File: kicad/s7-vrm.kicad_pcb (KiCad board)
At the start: 2 copper layers, 61.5 x 53 mm, 35 parts, among them J1 Conn_02x15_Row_Letter_First, Q1 Q_NPN_BEC, Q2 Q_NMOS_GDS, Q3 Q_NMOS_GDS, SW1 SW_DIP_x04, U1 NCP1579

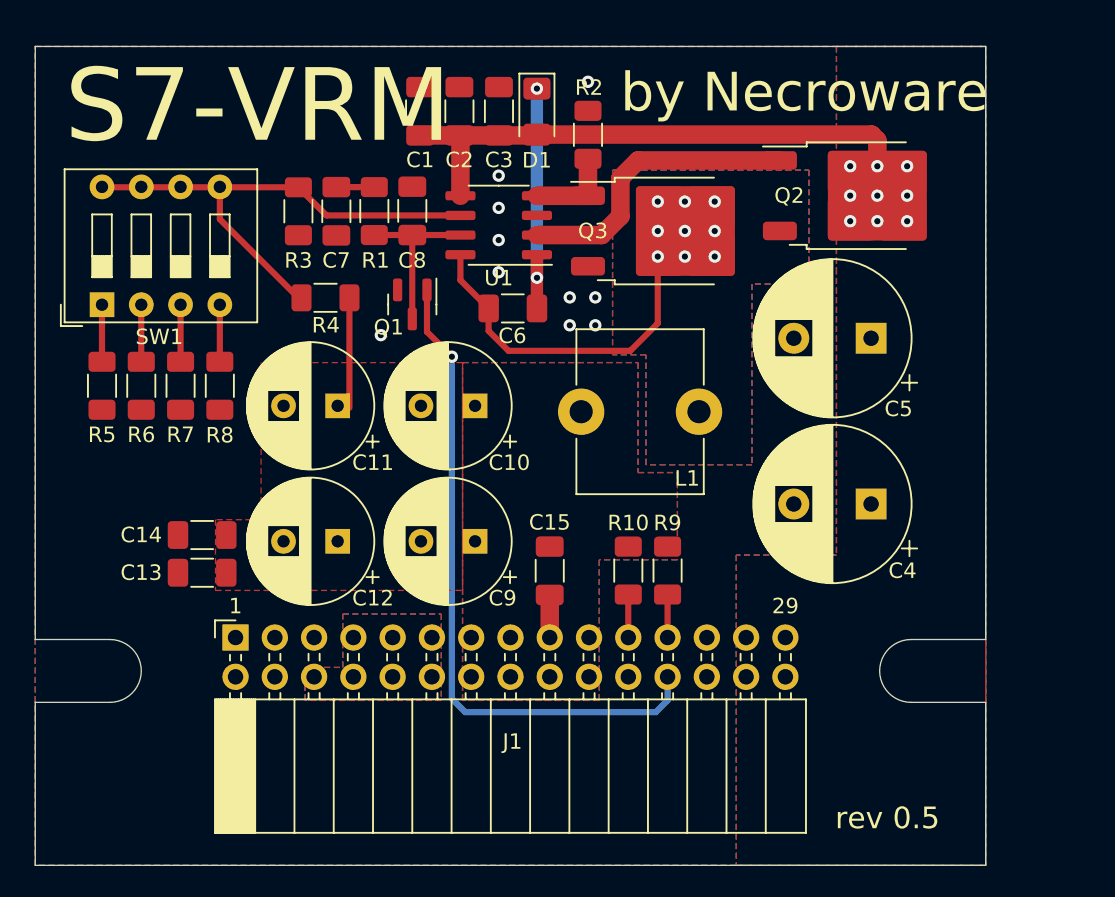
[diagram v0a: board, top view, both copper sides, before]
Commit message: Using sence to FB and transistor for PWRGOOD
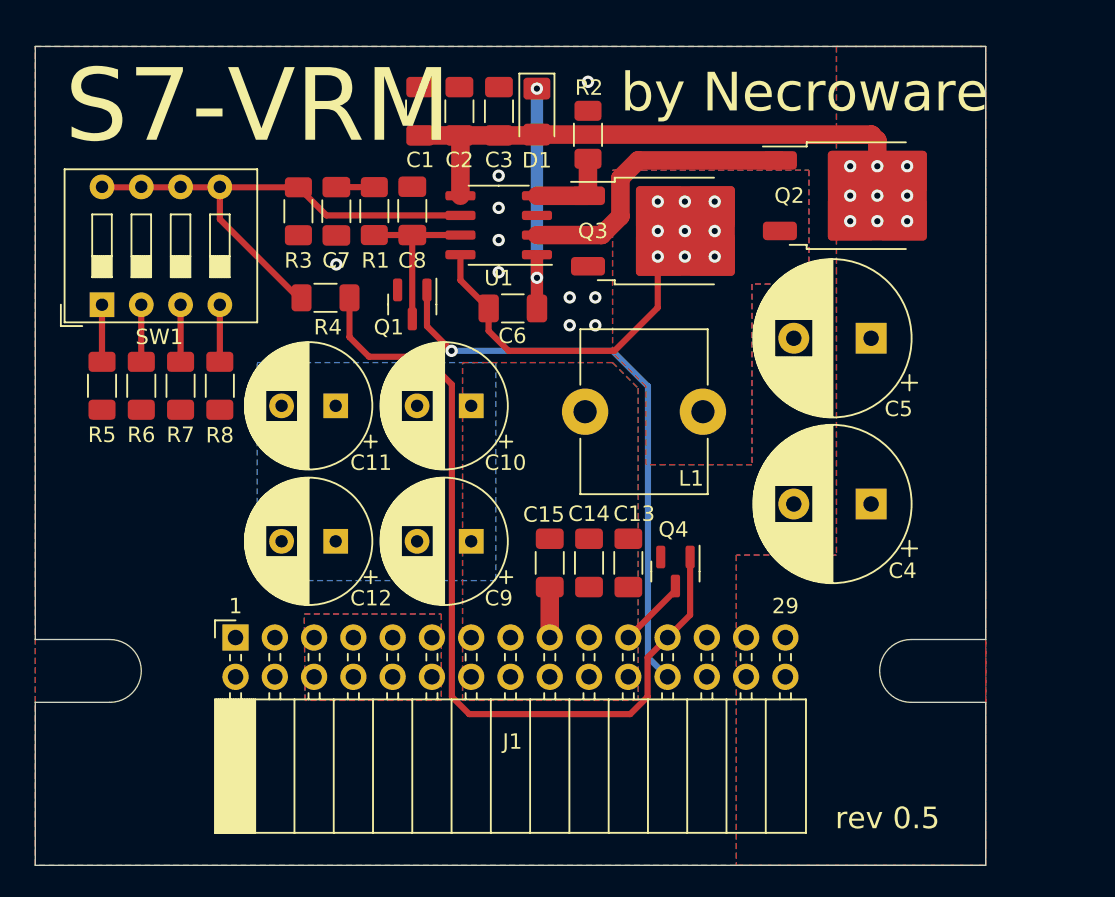
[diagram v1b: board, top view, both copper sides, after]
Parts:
- removed R10: 1K, Resistor_SMD:R_1206_3216Metric_Pad1.30x1.75mm_HandSolder
- removed R9: 0, Resistor_SMD:R_1206_3216Metric_Pad1.30x1.75mm_HandSolder
- added Q4: Q_NPN_BEC, Package_TO_SOT_SMD:SOT-23, F.Cu at (160.8, 114.1)
- moved C13 27.6 mm to (157.7, 113.5), turned to -90 degrees
- moved C14 25.1 mm to (155.2, 113.5), turned to -90 degrees
- moved C15 0.51 mm to (152.7, 113.5)
- moved L1 0.25 mm to (162.6, 103.8)
- moved C10 0.25 mm to (147.6, 103.4)
- moved C9 0.25 mm to (147.6, 112.1)
- moved REF** 0.13 mm to (171.3, 86.6)
- moved C11 0.13 mm to (138.8, 103.4)
- moved C12 0.13 mm to (138.8, 112.1)
- turned R4 to 0 degrees
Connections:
- R4 pad 1: VCORE -> FB
- R4 pad 2: FB -> SENSE
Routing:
- net SENSE: track 2.78 -> 54.4 mm
- net VCORE: track 7.16 -> 0.00 mm
- net DISABLE: track 43.3 -> 37.6 mm
- net PWRGOOD: track 2.78 -> 4.59 mm
- net /PHASE: track 22.2 -> 21.6 mm

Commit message: Work in progress
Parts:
- Q1: value Q_NPN_BEC -> Q_NPN_BEC_BRT
- Q4: value Q_NPN_BEC -> Q_PNP_BEC_BRT
- moved C13 0.38 mm to (157.7, 113.9)
- moved C14 0.38 mm to (155.2, 113.9)
- moved C15 0.38 mm to (152.7, 113.9)
- moved Q4 0.38 mm to (160.8, 114.5), turned to 90 degrees
- turned R4 to 180 degrees
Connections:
- Q4 pad 1: SENSE -> VCORE
- R4 pad 1: FB -> SENSE
- R4 pad 2: SENSE -> FB
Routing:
- net SENSE: track 54.4 -> 48.6 mm
- net GND: track 2.76 -> 7.84 mm
- net VCORE: track 0.00 -> 4.57 mm
- net PWRGOOD: track 4.59 -> 6.61 mm

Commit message: Prepared for production
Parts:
- moved C10 0.31 mm to (147.9, 103.4)
- moved C9 0.31 mm to (147.9, 112.1)
- moved R4 0.20 mm to (137.9, 96.4)
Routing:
- net GND: track 7.84 -> 2.88 mm

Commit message: Update LCSC parts and values
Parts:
- C7: value 330n -> 242n
- C8: value 47p -> 39p
- R1, R2, R5: value 12K -> 15K
- R3: value 3K -> 5K
- R6: value 6K -> 7,5K
- R7: value 4,8K -> 6K
- R8: value 3K -> 3,75K
- U1: value NCP1579 -> ISL6545
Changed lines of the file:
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@@
     (descr "Resistor SMD 1206 (3216 Metric), square (rectangular) end terminal, IPC_7351 nominal with elongated pad for handsoldering. (Body size source: IPC-SM-782 page 72, https://www.pcb-3d.com/wordpress/wp-content/uploads/ipc-sm-782a_amendment_1_and_2.pdf), generated with kicad-footprint-generator")
     (tags "resistor handsolder")
-    (property "LCSC" "C2930406")
+    (property "LCSC" "C136874")
     (property "Sheetfile" "s7-vrm.kicad_sch")
     (property "Sheetname" "")
@@
         (effects (font (size 1 1) (thickness 0.15)))
     )
-    (fp_text value "12K" (at 0 1.82 90) (layer "F.Fab")
+    (fp_text value "15K" (at 0 1.82 90) (layer "F.Fab")
         (effects (font (size 1 1) (thickness 0.15)))
     )
@@
     (descr "Resistor SMD 1206 (3216 Metric), square (rectangular) end terminal, IPC_7351 nominal with elongated pad for handsoldering. (Body size source: IPC-SM-782 page 72, https://www.pcb-3d.com/wordpress/wp-content/uploads/ipc-sm-782a_amendment_1_and_2.pdf), generated with kicad-footprint-generator")
     (tags "resistor handsolder")
-    (property "LCSC" "C3000586")
+    (property "LCSC" "C137115")
     (property "Sheetfile" "s7-vrm.kicad_sch")
     (property "Sheetname" "")
@@
         (effects (font (size 1 1) (thickness 0.15)))
     )
-    (fp_text value "6K" (at 0 1.82 -270) (layer "F.Fab")
+    (fp_text value "7,5K" (at 0 1.82 -270) (layer "F.Fab")
         (effects (font (size 1 1) (thickness 0.15)))
     )
@@
     (descr "Resistor SMD 1206 (3216 Metric), square (rectangular) end terminal, IPC_7351 nominal with elongated pad for handsoldering. (Body size source: IPC-SM-782 page 72, https://www.pcb-3d.com/wordpress/wp-content/uploads/ipc-sm-782a_amendment_1_and_2.pdf), generated with kicad-footprint-generator")
     (tags "resistor handsolder")
-    (property "LCSC" "C2930406")
+    (property "LCSC" "C136874")
     (property "Sheetfile" "s7-vrm.kicad_sch")
     (property "Sheetname" "")
@@
         (effects (font (size 1 1) (thickness 0.15)))
     )
-    (fp_text value "12K" (at 0 1.82 90) (layer "F.Fab")
+    (fp_text value "15K" (at 0 1.82 90) (layer "F.Fab")
         (effects (font (size 1 1) (thickness 0.15)))
     )
@@
     (descr "Capacitor SMD 1206 (3216 Metric), square (rectangular) end terminal, IPC_7351 nominal with elongated pad for handsoldering. (Body size source: IPC-SM-782 page 76, https://www.pcb-3d.com/wordpress/wp-content/uploads/ipc-sm-782a_amendment_1_and_2.pdf), generated with kicad-footprint-generator")
     (tags "capacitor handsolder")
-    (property "LCSC" "C107176")
+    (property "LCSC" "C577176")
     (property "Sheetfile" "s7-vrm.kicad_sch")
     (property "Sheetname" "")
@@
         (effects (font (size 1 1) (thickness 0.15)))
     )
-    (fp_text value "47p" (at 0 1.85 90) (layer "F.Fab")
+    (fp_text value "39p" (at 0 1.85 90) (layer "F.Fab")
         (effects (font (size 1 1) (thickness 0.15)))
     )
@@
     (descr "Resistor SMD 1206 (3216 Metric), square (rectangular) end terminal, IPC_7351 nominal with elongated pad for handsoldering. (Body size source: IPC-SM-782 page 72, https://www.pcb-3d.com/wordpress/wp-content/uploads/ipc-sm-782a_amendment_1_and_2.pdf), generated with kicad-footprint-generator")
     (tags "resistor handsolder")
-    (property "LCSC" "C488840")
+    (property "LCSC" "C870859")
     (property "Sheetfile" "s7-vrm.kicad_sch")
     (property "Sheetname" "")
@@
         (effects (font (size 1 1) (thickness 0.15)))
     )
-    (fp_text value "4,8K" (at 0 1.82 -270) (layer "F.Fab")
+    (fp_text value "6K" (at 0 1.82 -270) (layer "F.Fab")
         (effects (font (size 1 1) (thickness 0.15)))
     )
@@
     (descr "Resistor SMD 1206 (3216 Metric), square (rectangular) end terminal, IPC_7351 nominal with elongated pad for handsoldering. (Body size source: IPC-SM-782 page 72, https://www.pcb-3d.com/wordpress/wp-content/uploads/ipc-sm-782a_amendment_1_and_2.pdf), generated with kicad-footprint-generator")
     (tags "resistor handsolder")
-    (property "LCSC" "C229609")
+    (property "LCSC" "C132648")
     (property "Sheetfile" "s7-vrm.kicad_sch")
     (property "Sheetname" "")
@@
     (descr "Resistor SMD 1206 (3216 Metric), square (rectangular) end terminal, IPC_7351 nominal with elongated pad for handsoldering. (Body size source: IPC-SM-782 page 72, https://www.pcb-3d.com/wordpress/wp-content/uploads/ipc-sm-782a_amendment_1_and_2.pdf), generated with kicad-footprint-generator")
     (tags "resistor handsolder")
-    (property "LCSC" "C229609")
+    (property "LCSC" "C706412")
     (property "Sheetfile" "s7-vrm.kicad_sch")
     (property "Sheetname" "")
@@
         (effects (font (size 1 1) (thickness 0.15)))
     )
-    (fp_text value "3K" (at 0 1.82 -270) (layer "F.Fab")
+    (fp_text value "3,75K" (at 0 1.82 -270) (layer "F.Fab")
         (effects (font (size 1 1) (thickness 0.15)))
     )
@@
     (descr "Resistor SMD 1206 (3216 Metric), square (rectangular) end terminal, IPC_7351 nominal with elongated pad for handsoldering. (Body size source: IPC-SM-782 page 72, https://www.pcb-3d.com/wordpress/wp-content/uploads/ipc-sm-782a_amendment_1_and_2.pdf), generated with kicad-footprint-generator")
     (tags "resistor handsolder")
-    (property "LCSC" "C229609")
+    (property "LCSC" "C870818")
     (property "Sheetfile" "s7-vrm.kicad_sch")
     (property "Sheetname" "")
@@
         (effects (font (size 1 1) (thickness 0.15)))
     )
-    (fp_text value "3K" (at 0 1.82 90) (layer "F.Fab")
+    (fp_text value "5K" (at 0 1.82 90) (layer "F.Fab")
         (effects (font (size 1 1) (thickness 0.15)))
     )
@@
     (descr "Capacitor SMD 1206 (3216 Metric), square (rectangular) end terminal, IPC_7351 nominal with elongated pad for handsoldering. (Body size source: IPC-SM-782 page 76, https://www.pcb-3d.com/wordpress/wp-content/uploads/ipc-sm-782a_amendment_1_and_2.pdf), generated with kicad-footprint-generator")
     (tags "capacitor handsolder")
-    (property "LCSC" "C274377")
+    (property "LCSC" "C107186")
     (property "Sheetfile" "s7-vrm.kicad_sch")
     (property "Sheetname" "")
@@
         (effects (font (size 1 1) (thickness 0.15)))
     )
-    (fp_text value "330n" (at 0 1.85 90) (layer "F.Fab")
+    (fp_text value "242n" (at 0 1.85 90) (layer "F.Fab")
         (effects (font (size 1 1) (thickness 0.15)))
     )
@@
     (descr "SOIC, 8 Pin (JEDEC MS-012AA, https://www.analog.com/media/en/package-pcb-resources/package/pkg_pdf/soic_narrow-r/r_8.pdf), generated with kicad-footprint-generator ipc_gullwing_generator.py")
     (tags "SOIC SO")
-    (property "LCSC" "C235991")
+    (property "LCSC" "C382017")
     (property "Sheetfile" "s7-vrm.kicad_sch")
     (property "Sheetname" "")
@@
         (effects (font (size 1 1) (thickness 0.15)))
     )
-    (fp_text value "NCP1579" (at 0 3.4) (layer "F.Fab")
+    (fp_text value "ISL6545" (at 0 3.4) (layer "F.Fab")
         (effects (font (size 1 1) (thickness 0.15)))
     )
@@
     (descr "Resistor SMD 1206 (3216 Metric), square (rectangular) end terminal, IPC_7351 nominal with elongated pad for handsoldering. (Body size source: IPC-SM-782 page 72, https://www.pcb-3d.com/wordpress/wp-content/uploads/ipc-sm-782a_amendment_1_and_2.pdf), generated with kicad-footprint-generator")
     (tags "resistor handsolder")
-    (property "LCSC" "C2930406")
+    (property "LCSC" "C136874")
     (property "Sheetfile" "s7-vrm.kicad_sch")
     (property "Sheetname" "")
@@
         (effects (font (size 1 1) (thickness 0.15)))
     )
-    (fp_text value "12K" (at 0 1.82 -270) (layer "F.Fab")
+    (fp_text value "15K" (at 0 1.82 -270) (layer "F.Fab")
         (effects (font (size 1 1) (thickness 0.15)))
     )

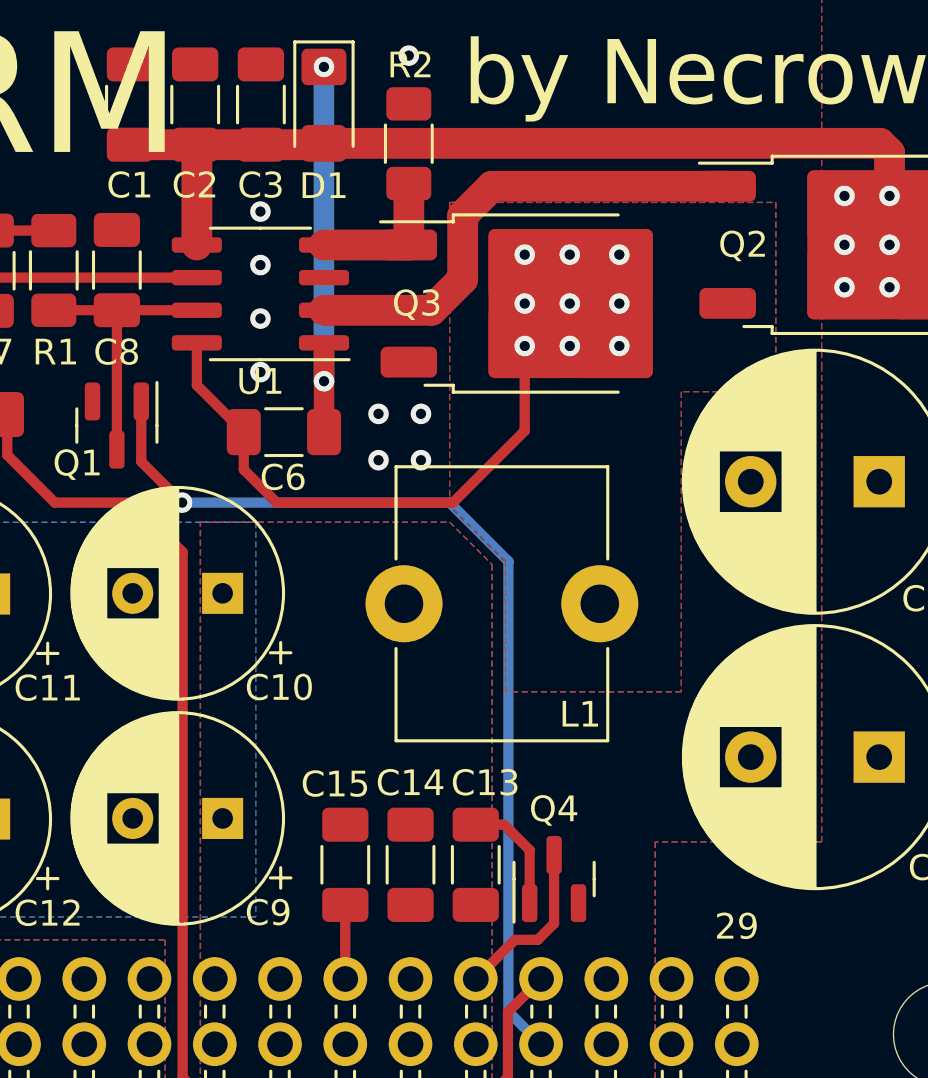
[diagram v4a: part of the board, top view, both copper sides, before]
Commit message: Swap R3 and R4 to get proper voltage
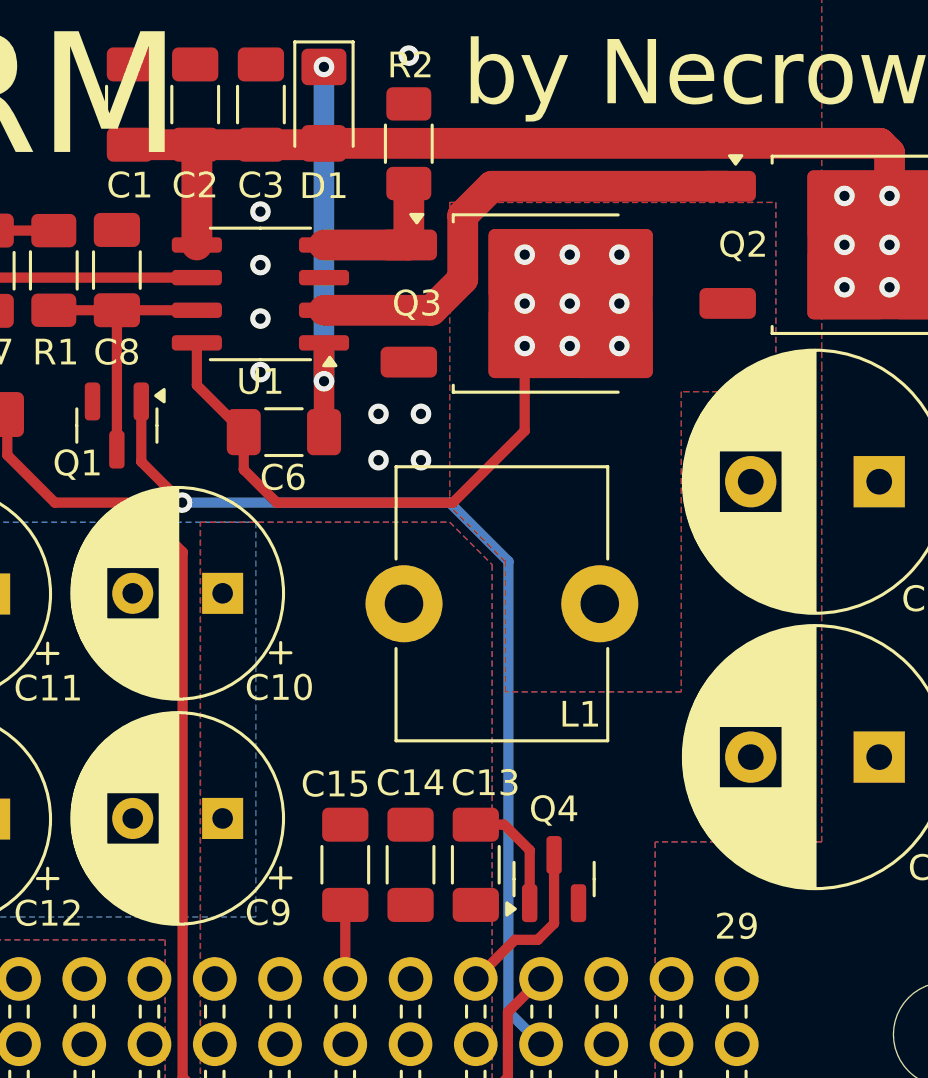
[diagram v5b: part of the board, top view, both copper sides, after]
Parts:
- R3: value 5K -> 3K
- R4: value 3K -> 5K

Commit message: prepare rev 0.6
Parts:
- added J2: Conn_02x02_Odd_Even, Connector_PinHeader_2.54mm:PinHeader_2x02_P2.54mm_Vertical, F.Cu at (131.2, 112.1)
- added R9: 3,75K, Resistor_SMD:R_1206_3216Metric_Pad1.30x1.75mm_HandSolder, F.Cu at (132.5, 102.8)
- R3: value 3K -> 3,75K
- R5: value 15K -> 30K
- R6: value 7,5K -> 15K
- R7: value 6K -> 7,5K
- SW1: footprint Button_Switch_THT:SW_DIP_SPSTx04_Slide_9.78x12.34mm_W7.62mm_P2.54mm -> Button_Switch_THT:SW_DIP_SPSTx05_Slide_9.78x14.88mm_W7.62mm_P2.54mm
- moved REF** 47.0 mm to (127.4, 103.2)
- moved G*** 10.3 mm to (172.3, 104.4)
- moved C13 3.12 mm to (159.1, 111.1), turned to 0 degrees
- moved Q4 2.03 mm to (158.8, 114.5)
- moved R8 1.59 mm to (129.9, 102.8)
- moved R6 1.59 mm to (124.8, 102.8)
- moved R5 1.59 mm to (122.3, 102.8)
- moved R7 1.59 mm to (127.4, 102.8)
- moved SW1 1.40 mm to (122.3, 96.8)
- moved C4 1.02 mm to (173.4, 110.7)
- moved C11 1.02 mm to (139.8, 103.4)
- moved C12 1.02 mm to (139.8, 112.1)
- moved C10 0.76 mm to (148.6, 103.4)
- moved C9 0.76 mm to (148.6, 112.1)
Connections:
- J1 pad 6: +3.3V -> VIO
- J1 pad 7: +3.3V -> VIO
- J1 pad 8: +3.3V -> VIO
- SW1 pad 5: FB -> Net-(R9-Pad1)
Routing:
- net SENSE: track 48.4 -> 39.0 mm, vias 0 -> 1
- net VCORE: track 4.57 -> 0.00 mm
- net Net-(R9-Pad1): track 0.00 -> 4.45 mm
- net FB: track 32.7 -> 35.9 mm
- net PWRGOOD: track 6.61 -> 5.25 mm
- net DISABLE: track 37.6 -> 38.6 mm
- net Net-(R8-Pad1): track 3.69 -> 4.45 mm
- net Net-(R7-Pad1): track 3.69 -> 4.45 mm
- net Net-(R6-Pad1): track 3.69 -> 4.45 mm
- net Net-(R5-Pad1): track 3.69 -> 4.45 mm
- net GND: vias 10 -> 18
- added copper zone on F.Cu, net VIO
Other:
- board size 61.5 x 53 mm -> 61.7 x 53 mm
- board text added: "1.40V:00000 | 2.00V:01100 | 2.90V:11110 SW1 voltage 1.50V:10000 | 2.10V:11100 | 3.00V:00011 1: on 1.60V:01000 | 2.20V:00010 | 3.10V:10011 0: off 1.70V:11000 | 2.30V:10010 | 3.20V:01011 1.80V:00100 | 2.40V:01010 | 3.30V:11011 1.90V:10100 | 2.50V:11010 | 3.40V:00111 | 2.60V:00110 | 3.50V:10111 | 2.70V:10110 | 3.60V:01111 | 2.80V:01110 | 3.70V:11111"
- board text added: "J1 voltage type 1-2,3-4:dual 1-3,2-4:single"
- board text removed: "SW1 Settings: 1.6V: 0000 | 2.6V: 1001 1.8V: 1000 | 2.7V: 1110 2.0V: 0100 | 2.8V: 0101 2.1V: 0010 | 2.9V: 0011 2.2V: 1100 | 3.0V: 1101 2.3V: 1010 | 3.1V: 1011 2.4V: 0001 | 3.3V: 0111 2.5V: 0110 | 3.5V: 1111"
